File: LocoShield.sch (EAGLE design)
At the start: 27 parts, among them J2 RJ12/6, J3 RJ12/6, Q1 2N3904, U1 LM393M, U2 LM317LCDR

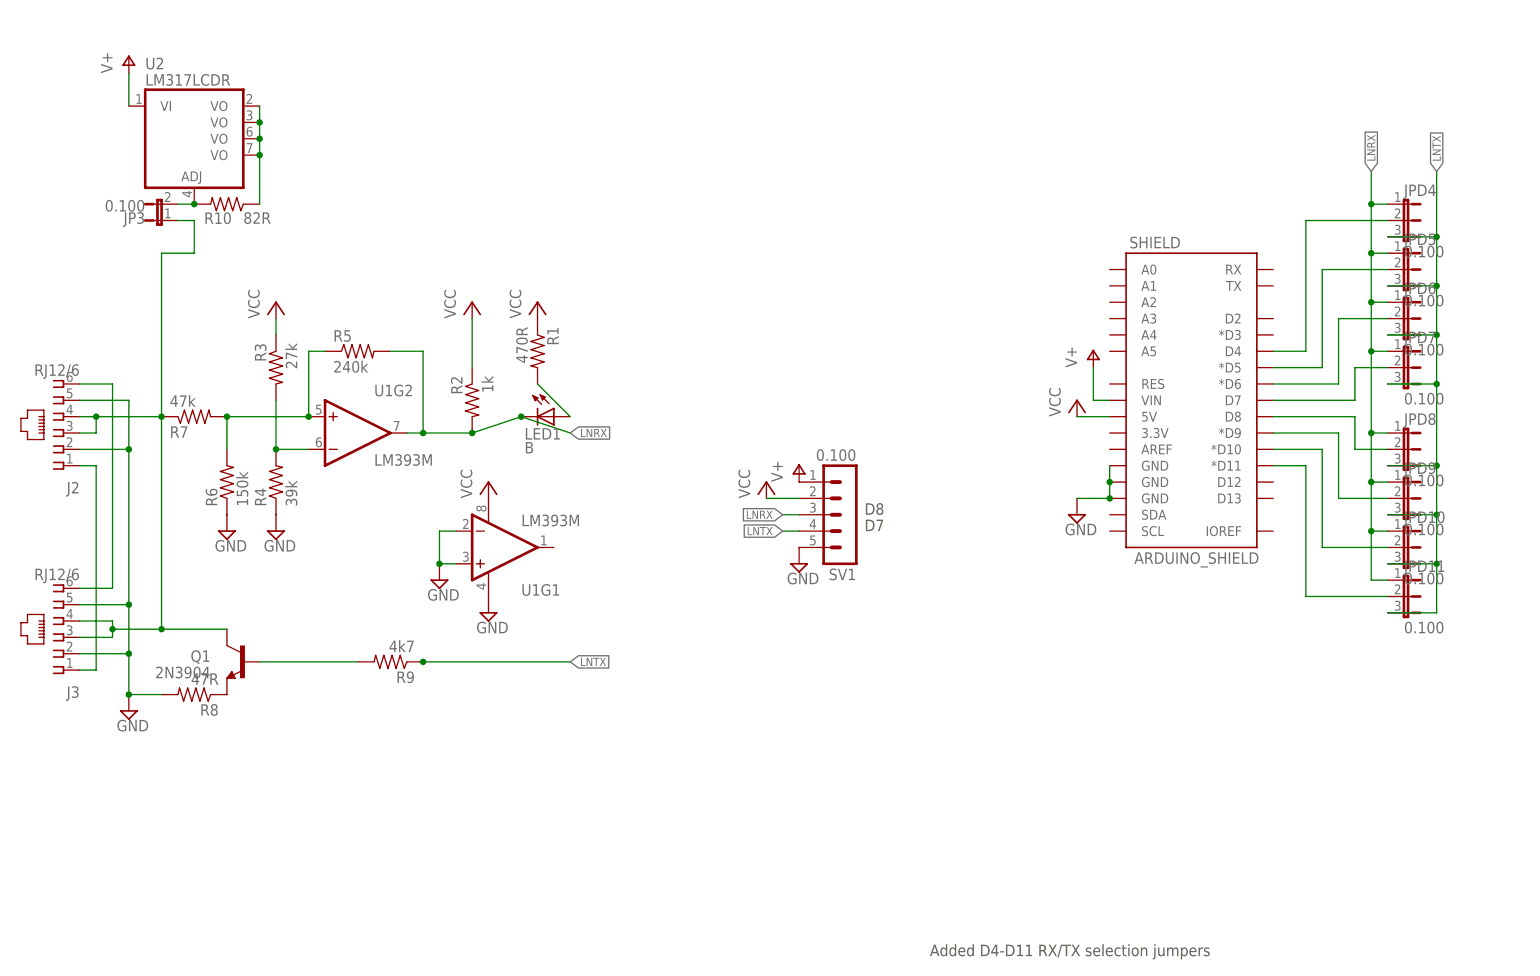
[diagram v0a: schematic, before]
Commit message: moved away from shield form
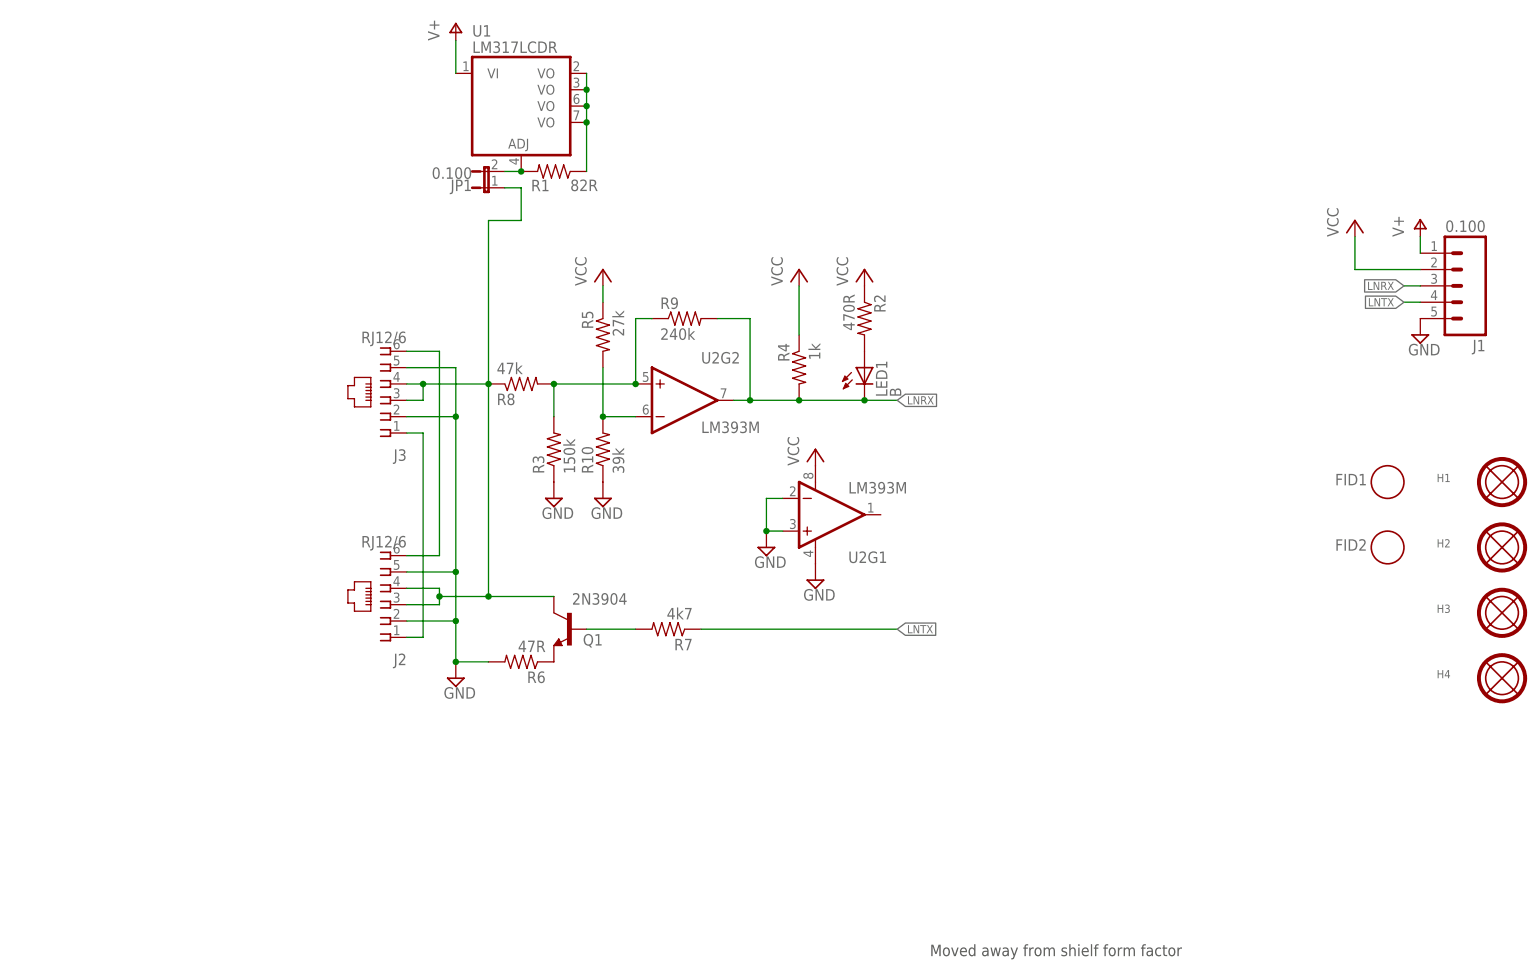
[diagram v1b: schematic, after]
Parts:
- removed JP3: 0.100, MCP:JUMPER-2PTH_LOCK
- removed JPD10, JPD11, JPD4, JPD5, JPD6, JPD7, JPD8, JPD9: 0.100, MCP:JP2E
- removed SHIELD: ARDUINO_SHIELD, SPCoast:ARDUINO_SHIELDNO_SILK
- removed SV1: 0.100, con-lstb:MA05-1
- added FID1, FID2: FIDUCIAL, SPCoast:FIDUCIAL
- added H1, H2, H3, H4: MOUNTINGHOLEL, SPCoast:MOUNTINGHOLEL
- added J1: 0.100, SPCoast:CONNECTOR-M05LOCK
- added JP1: 0.100, SPCoast:JUMPER-2PTH_LOCK
- Q1: device MCP:NPN-SOT23-3 -> SPCoast:NPN-SOT23
- R1: value 470R -> 82R
- R10: value 82R -> 39k; device SPCoast:R0805-RES -> SPCoast:R0603-RES
- R2: value 1k -> 470R
- R3: value 27k -> 150k
- R4: value 39k -> 1k
- R5: value 240k -> 27k
- R6: value 150k -> 47R
- R7: value 47k -> 4k7
- R8: value 47R -> 47k
- R9: value 4k7 -> 240k
- U1: value LM393M -> LM317LCDR; device MCP:LM393M -> SPCoast:LM317LD
- U2: value LM317LCDR -> LM393M; device MCP:LM317LD -> SPCoast:LM393M
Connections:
- removed net D10: JPD10.2, SHIELD.*D10
- removed net D11: JPD11.2, SHIELD.*D11
- removed net D4: JPD4.2, SHIELD.D4
- removed net D5: JPD5.2, SHIELD.*D5
- removed net D6: JPD6.2, SHIELD.*D6
- removed net D7: JPD7.2, SHIELD.D7
- removed net D8: JPD8.2, SHIELD.D8
- removed net D9: JPD9.2, SHIELD.*D9
- net GND: now also J1.5, R10.1, R3.1, R6.2, U2G1.+IN, U2G1.-IN, U2G1.V-; no longer R4.1, R6.1, R8.2, SHIELD.GND@0, SHIELD.GND@1, SHIELD.GND@2, SV1.5, U1G1.+IN, U1G1.-IN, U1G1.V-
- net LNRX: now also J1.3, R4.2, R9.2, U2G2.OUT; no longer JPD10.1, JPD11.1, JPD4.1, JPD5.1, JPD6.1, JPD7.1, JPD8.1, JPD9.1, R2.2, R5.2, SV1.3, U1G2.OUT
- net LNTX: now also J1.4, R7.1; no longer JPD10.3, JPD11.3, JPD4.3, JPD5.3, JPD6.3, JPD7.3, JPD8.3, JPD9.3, R9.1, SV1.4
- net LOCONET: now also JP1.1, R8.1; no longer JP3.1, R7.1
- net N$1: now also R7.2; no longer R9.2
- net N$15: now also R2.2; no longer R1.2
- net N$2: now also R3.2, R8.2, R9.1, U2G2.+IN; no longer R5.1, R6.2, R7.2, U1G2.+IN
- net N$20: now also JP1.2, R1.2, U1.ADJ; no longer JP3.2, R10.2, U2.ADJ
- net N$5: now also R10.2, R5.2, U2G2.-IN; no longer R3.2, R4.2, U1G2.-IN
- net N$6: now also R6.1; no longer R8.1
- net V+: now also J1.1, U1.VI; no longer SHIELD.VIN, SV1.1, U2.VI
- net VCC: now also J1.2, R4.1, R5.1, U2G1.V+; no longer R1.1, R3.1, SHIELD.5V, SV1.2, U1G1.V+
- net VOUT: now also R1.1, U1.VO, U1.VO@1, U1.VO@2, U1.VO@3; no longer R10.1, U2.VO, U2.VO@1, U2.VO@2, U2.VO@3
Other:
- note added: "+12v"
- note added: "+5v"
- note added: "2.0"
- note added: "Loconet Termination (Optional)"
- note added: "Moved away from shielf form factor"
- note removed: "1.4"
- note removed: "Added D4-D11 RX/TX selection jumpers"
- note removed: "D7"
- note removed: "D8"
- moved on the sheet: J2, J3, LED1, R1, R10, R2, R3, R4, R5, R6, R7, R8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

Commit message: Version 2.0
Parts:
- renumbered FID1 to FIDUL, FID2 to FIDLR
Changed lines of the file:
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@@
 <part name="H1" library="SPCoast" deviceset="MOUNTINGHOLE" device="L"/>
 <part name="J1" library="SPCoast" deviceset="CONNECTOR-M05" device="LOCK" value="0.100"/>
-<part name="FID1" library="SPCoast" deviceset="FIDUCIAL" device=""/>
-<part name="FID2" library="SPCoast" deviceset="FIDUCIAL" device=""/>
+<part name="FIDUL" library="SPCoast" deviceset="FIDUCIAL" device=""/>
+<part name="FIDLR" library="SPCoast" deviceset="FIDUCIAL" device=""/>
 </parts>
 <sheets>
@@
 <instance part="H1" gate="MT1" x="241.3" y="81.28"/>
 <instance part="J1" gate="CON1" x="236.22" y="111.76" rot="R180"/>
-<instance part="FID1" gate="FID1" x="223.52" y="81.28"/>
-<instance part="FID2" gate="FID1" x="223.52" y="71.12"/>
+<instance part="FIDUL" gate="FID1" x="223.52" y="81.28"/>
+<instance part="FIDLR" gate="FID1" x="223.52" y="71.12"/>
 </instances>
 <busses>

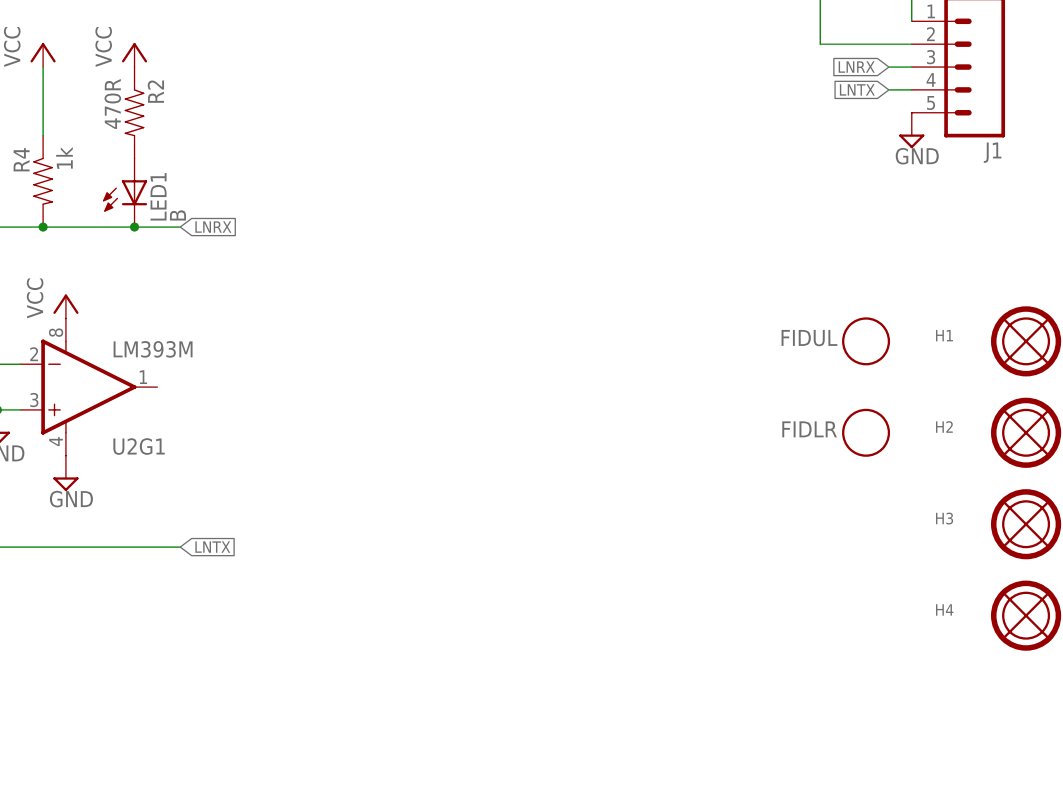
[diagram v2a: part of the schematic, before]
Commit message: added tooling for JLC
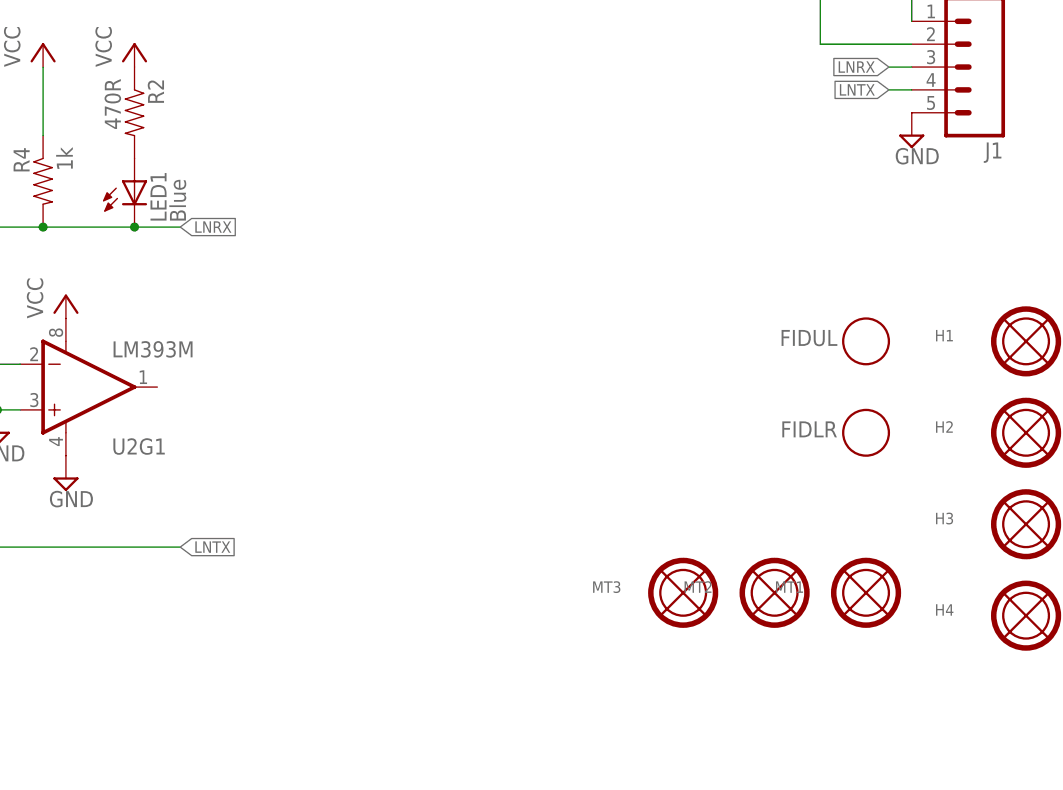
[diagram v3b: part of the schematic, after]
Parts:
- added MT1, MT2, MT3: tool, SPCoast:MOUNTINGHOLET
- H1, H2, H3, H4: value MOUNTINGHOLEL -> (none)
- LED1: value B -> Blue
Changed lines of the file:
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@@
 <grid distance="100" unitdist="mil" unit="mil" style="dots" multiple="1" display="yes" altdistance="50" altunitdist="mil" altunit="mil"/>
 <layers>
-<layer number="1" name="Top" color="4" fill="1" visible="yes" active="no"/>
-<layer number="2" name="Route2" color="1" fill="3" visible="yes" active="no"/>
-<layer number="3" name="Route3" color="4" fill="3" visible="yes" active="no"/>
-<layer number="4" name="Route4" color="1" fill="4" visible="yes" active="no"/>
-<layer number="5" name="Route5" color="4" fill="4" visible="yes" active="no"/>
-<layer number="6" name="Route6" color="1" fill="8" visible="yes" active="no"/>
-<layer number="7" name="Route7" color="4" fill="8" visible="yes" active="no"/>
-<layer number="8" name="Route8" color="1" fill="2" visible="yes" active="no"/>
-<layer number="9" name="Route9" color="4" fill="2" visible="yes" active="no"/>
-<layer number="10" name="Route10" color="1" fill="7" visible="yes" active="no"/>
-<layer number="11" name="Route11" color="4" fill="7" visible="yes" active="no"/>
-<layer number="12" name="Route12" color="1" fill="5" visible="yes" active="no"/>
-<layer number="13" name="Route13" color="4" fill="5" visible="yes" active="no"/>
-<layer number="14" name="Route14" color="1" fill="6" visible="yes" active="no"/>
-<layer number="15" name="Route15" color="4" fill="6" visible="yes" active="no"/>
-<layer number="16" name="Bottom" color="2" fill="1" visible="yes" active="no"/>
-<layer number="17" name="Pads" color="23" fill="1" visible="yes" active="no"/>
-<layer number="18" name="Vias" color="29" fill="1" visible="yes" active="no"/>
-<layer number="19" name="Unrouted" color="6" fill="1" visible="yes" active="no"/>
-<layer number="20" name="Dimension" color="15" fill="1" visible="yes" active="no"/>
-<layer number="21" name="tPlace" color="36" fill="1" visible="yes" active="no"/>
-<layer number="22" name="bPlace" color="17" fill="1" visible="yes" active="no"/>
-<layer number="23" name="tOrigins" color="30" fill="1" visible="yes" active="no"/>
-<layer number="24" name="bOrigins" color="15" fill="1" visible="yes" active="no"/>
-<layer number="25" name="tNames" color="63" fill="1" visible="yes" active="no"/>
-<layer number="26" name="bNames" color="34" fill="1" visible="yes" active="no"/>
-<layer number="27" name="tValues" color="56" fill="1" visible="yes" active="no"/>
-<layer number="28" name="bValues" color="7" fill="1" visible="yes" active="no"/>
+<layer number="1" name="Top" color="4" fill="1" visible="no" active="no"/>
+<layer number="2" name="Route2" color="1" fill="3" visible="no" active="no"/>
+<layer number="3" name="Route3" color="4" fill="3" visible="no" active="no"/>
+<layer number="4" name="Route4" color="1" fill="4" visible="no" active="no"/>
+<layer number="5" name="Route5" color="4" fill="4" visible="no" active="no"/>
+<layer number="6" name="Route6" color="1" fill="8" visible="no" active="no"/>
+<layer number="7" name="Route7" color="4" fill="8" visible="no" active="no"/>
+<layer number="8" name="Route8" color="1" fill="2" visible="no" active="no"/>
+<layer number="9" name="Route9" color="4" fill="2" visible="no" active="no"/>
+<layer number="10" name="Route10" color="1" fill="7" visible="no" active="no"/>
+<layer number="11" name="Route11" color="4" fill="7" visible="no" active="no"/>
+<layer number="12" name="Route12" color="1" fill="5" visible="no" active="no"/>
+<layer number="13" name="Route13" color="4" fill="5" visible="no" active="no"/>
+<layer number="14" name="Route14" color="1" fill="6" visible="no" active="no"/>
+<layer number="15" name="Route15" color="4" fill="6" visible="no" active="no"/>
+<layer number="16" name="Bottom" color="2" fill="1" visible="no" active="no"/>
+<layer number="17" name="Pads" color="23" fill="1" visible="no" active="no"/>
+<layer number="18" name="Vias" color="29" fill="1" visible="no" active="no"/>
+<layer number="19" name="Unrouted" color="6" fill="1" visible="no" active="no"/>
+<layer number="20" name="Dimension" color="15" fill="1" visible="no" active="no"/>
+<layer number="21" name="tPlace" color="36" fill="1" visible="no" active="no"/>
+<layer number="22" name="bPlace" color="17" fill="1" visible="no" active="no"/>
+<layer number="23" name="tOrigins" color="30" fill="1" visible="no" active="no"/>
+<layer number="24" name="bOrigins" color="15" fill="1" visible="no" active="no"/>
+<layer number="25" name="tNames" color="63" fill="1" visible="no" active="no"/>
+<layer number="26" name="bNames" color="34" fill="1" visible="no" active="no"/>
+<layer number="27" name="tValues" color="56" fill="1" visible="no" active="no"/>
+<layer number="28" name="bValues" color="7" fill="1" visible="no" active="no"/>
 <layer number="29" name="tStop" color="7" fill="3" visible="no" active="no"/>
 <layer number="30" name="bStop" color="7" fill="6" visible="no" active="no"/>
@@
 <layer number="35" name="tGlue" color="7" fill="4" visible="no" active="no"/>
 <layer number="36" name="bGlue" color="7" fill="5" visible="no" active="no"/>
-<layer number="37" name="tTest" color="7" fill="1" visible="yes" active="no"/>
-<layer number="38" name="bTest" color="7" fill="1" visible="yes" active="no"/>
+<layer number="37" name="tTest" color="7" fill="1" visible="no" active="no"/>
+<layer number="38" name="bTest" color="7" fill="1" visible="no" active="no"/>
 <layer number="39" name="tKeepout" color="4" fill="11" visible="no" active="no"/>
 <layer number="40" name="bKeepout" color="3" fill="11" visible="no" active="no"/>
@@
 <layer number="44" name="Drills" color="16" fill="1" visible="no" active="no"/>
 <layer number="45" name="Holes" color="35" fill="1" visible="no" active="no"/>
-<layer number="46" name="Milling" color="35" fill="1" visible="yes" active="no"/>
-<layer number="47" name="Measures" color="21" fill="1" visible="yes" active="no"/>
-<layer number="48" name="Document" color="47" fill="1" visible="yes" active="no"/>
-<layer number="49" name="Reference" color="48" fill="1" visible="yes" active="no"/>
-<layer number="50" name="dxf" color="7" fill="1" visible="yes" active="no"/>
-<layer number="51" name="tDocu" color="24" fill="1" visible="yes" active="no"/>
-<layer number="52" name="bDocu" color="7" fill="1" visible="yes" active="no"/>
-<layer number="53" name="tGND_GNDA" color="7" fill="9" visible="yes" active="no"/>
-<layer number="54" name="bGND_GNDA" color="1" fill="9" visible="yes" active="no"/>
-<layer number="56" name="wert" color="7" fill="1" visible="yes" active="no"/>
-<layer number="57" name="tCAD" color="7" fill="1" visible="yes" active="no"/>
-<layer number="59" name="tCarbon" color="7" fill="1" visible="yes" active="no"/>
-<layer number="60" name="bCarbon" color="7" fill="1" visible="yes" active="no"/>
+<layer number="46" name="Milling" color="35" fill="1" visible="no" active="no"/>
+<layer number="47" name="Measures" color="21" fill="1" visible="no" active="no"/>
+<layer number="48" name="Document" color="47" fill="1" visible="no" active="no"/>
+<layer number="49" name="Reference" color="48" fill="1" visible="no" active="no"/>
+<layer number="50" name="dxf" color="7" fill="1" visible="no" active="no"/>
+<layer number="51" name="tDocu" color="24" fill="1" visible="no" active="no"/>
+<layer number="52" name="bDocu" color="7" fill="1" visible="no" active="no"/>
+<layer number="53" name="tGND_GNDA" color="7" fill="9" visible="no" active="no"/>
+<layer number="54" name="bGND_GNDA" color="1" fill="9" visible="no" active="no"/>
+<layer number="56" name="wert" color="7" fill="1" visible="no" active="no"/>
+<layer number="57" name="tCAD" color="7" fill="1" visible="no" active="no"/>
+<layer number="59" name="tCarbon" color="7" fill="1" visible="no" active="no"/>
+<layer number="60" name="bCarbon" color="7" fill="1" visible="no" active="no"/>
 <layer number="90" name="Modules" color="5" fill="1" visible="yes" active="yes"/>
 <layer number="91" name="Nets" color="2" fill="1" visible="yes" active="yes"/>
@@
 <part name="U2" library="SPCoast" deviceset="LM393" device="M"/>
 <part name="R6" library="SPCoast" deviceset="R*" device="0603-RES" value="47R"/>
-<part name="LED1" library="SPCoast" deviceset="LED*" device="0603-LED" value="B"/>
+<part name="LED1" library="SPCoast" deviceset="LED*" device="0603-LED" value="Blue"/>
 <part name="P+1" library="supply1" deviceset="VCC" device=""/>
 <part name="V3" library="supply2" deviceset="GND" device=""/>
@@
 <part name="FIDUL" library="SPCoast" deviceset="FIDUCIAL" device=""/>
 <part name="FIDLR" library="SPCoast" deviceset="FIDUCIAL" device=""/>
+<part name="MT1" library="SPCoast" deviceset="MOUNTINGHOLE" device="T" value="tool"/>
+<part name="MT2" library="SPCoast" deviceset="MOUNTINGHOLE" device="T" value="tool"/>
+<part name="MT3" library="SPCoast" deviceset="MOUNTINGHOLE" device="T" value="tool"/>
 </parts>
 <sheets>
@@
 <instance part="FIDUL" gate="FID1" x="223.52" y="81.28"/>
 <instance part="FIDLR" gate="FID1" x="223.52" y="71.12"/>
+<instance part="MT1" gate="MT1" x="223.52" y="53.34"/>
+<instance part="MT2" gate="MT1" x="213.36" y="53.34"/>
+<instance part="MT3" gate="MT1" x="203.2" y="53.34"/>
 </instances>
 <busses>
